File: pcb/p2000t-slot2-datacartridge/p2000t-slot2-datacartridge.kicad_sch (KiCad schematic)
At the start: 27 parts, among them J1 P2000T Port 2, U1 74HC04, U11 CY62256-70PC, U13 74HC173, U14 ZIF, U15 74HC02, U3 74HC138, U4 74HC21, U5 SST39SF040, U6 74HC02, U8 74HC273, U9 74HC273

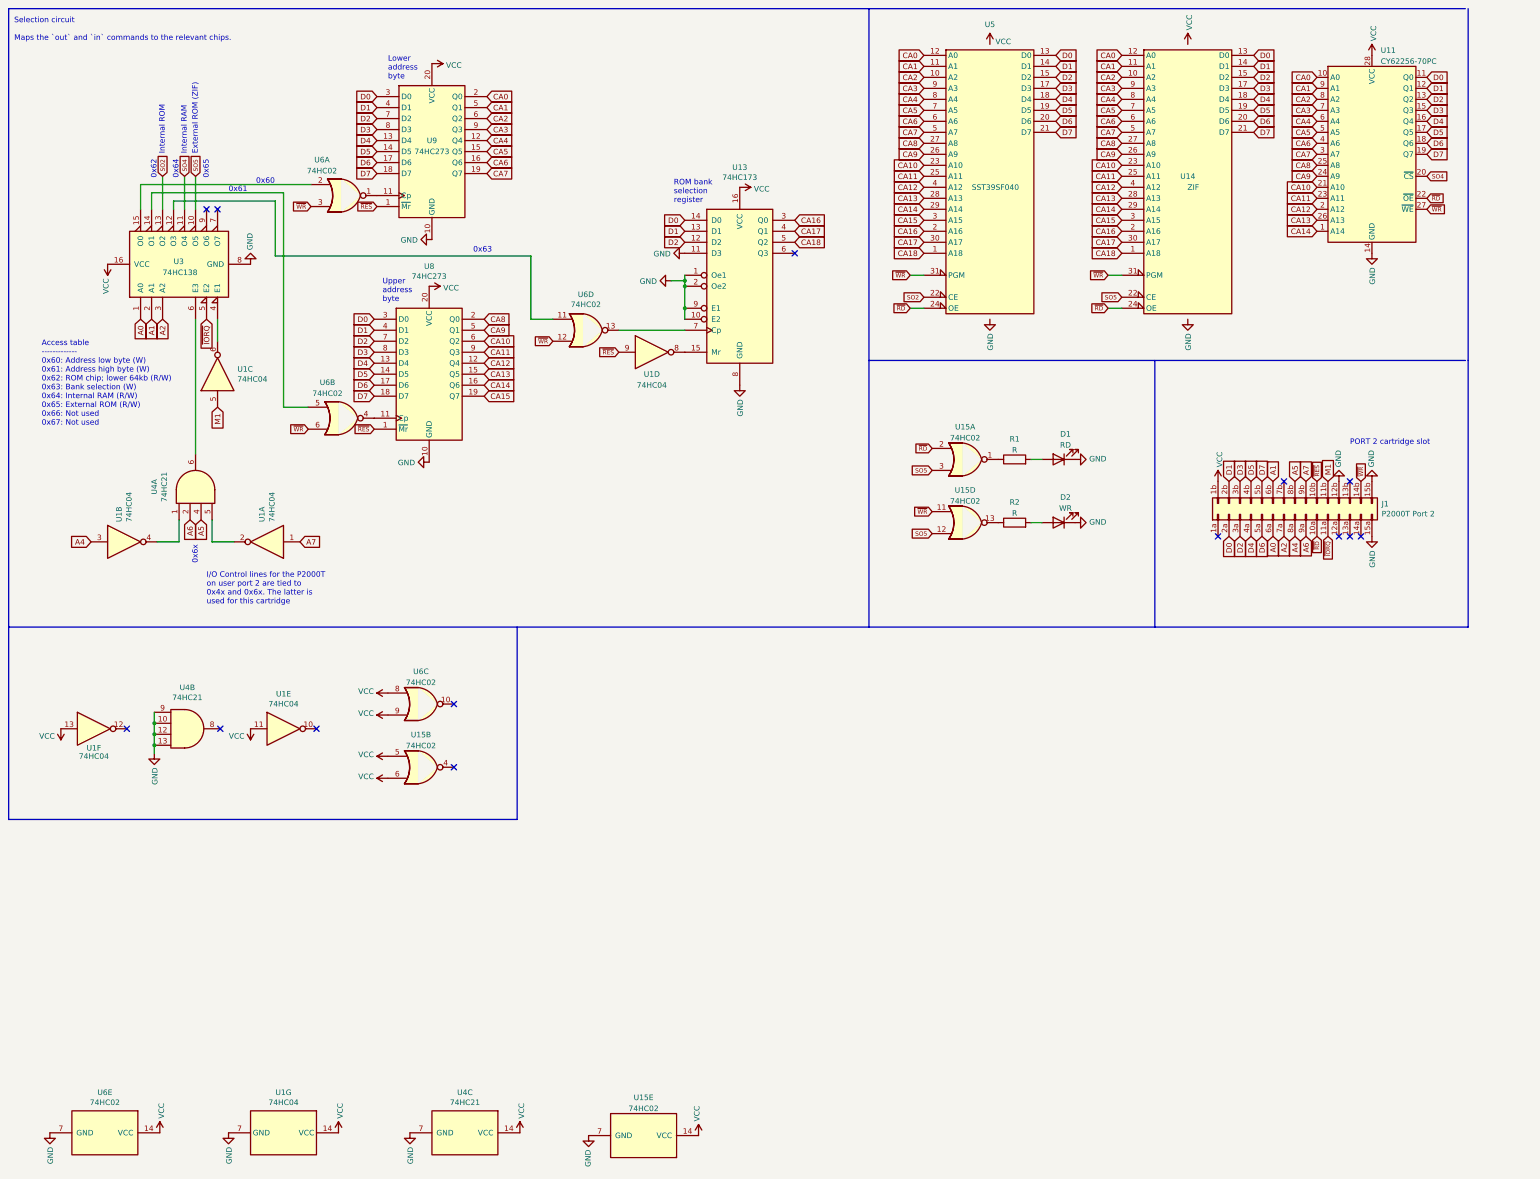
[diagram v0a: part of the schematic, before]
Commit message: Improving lay-out board
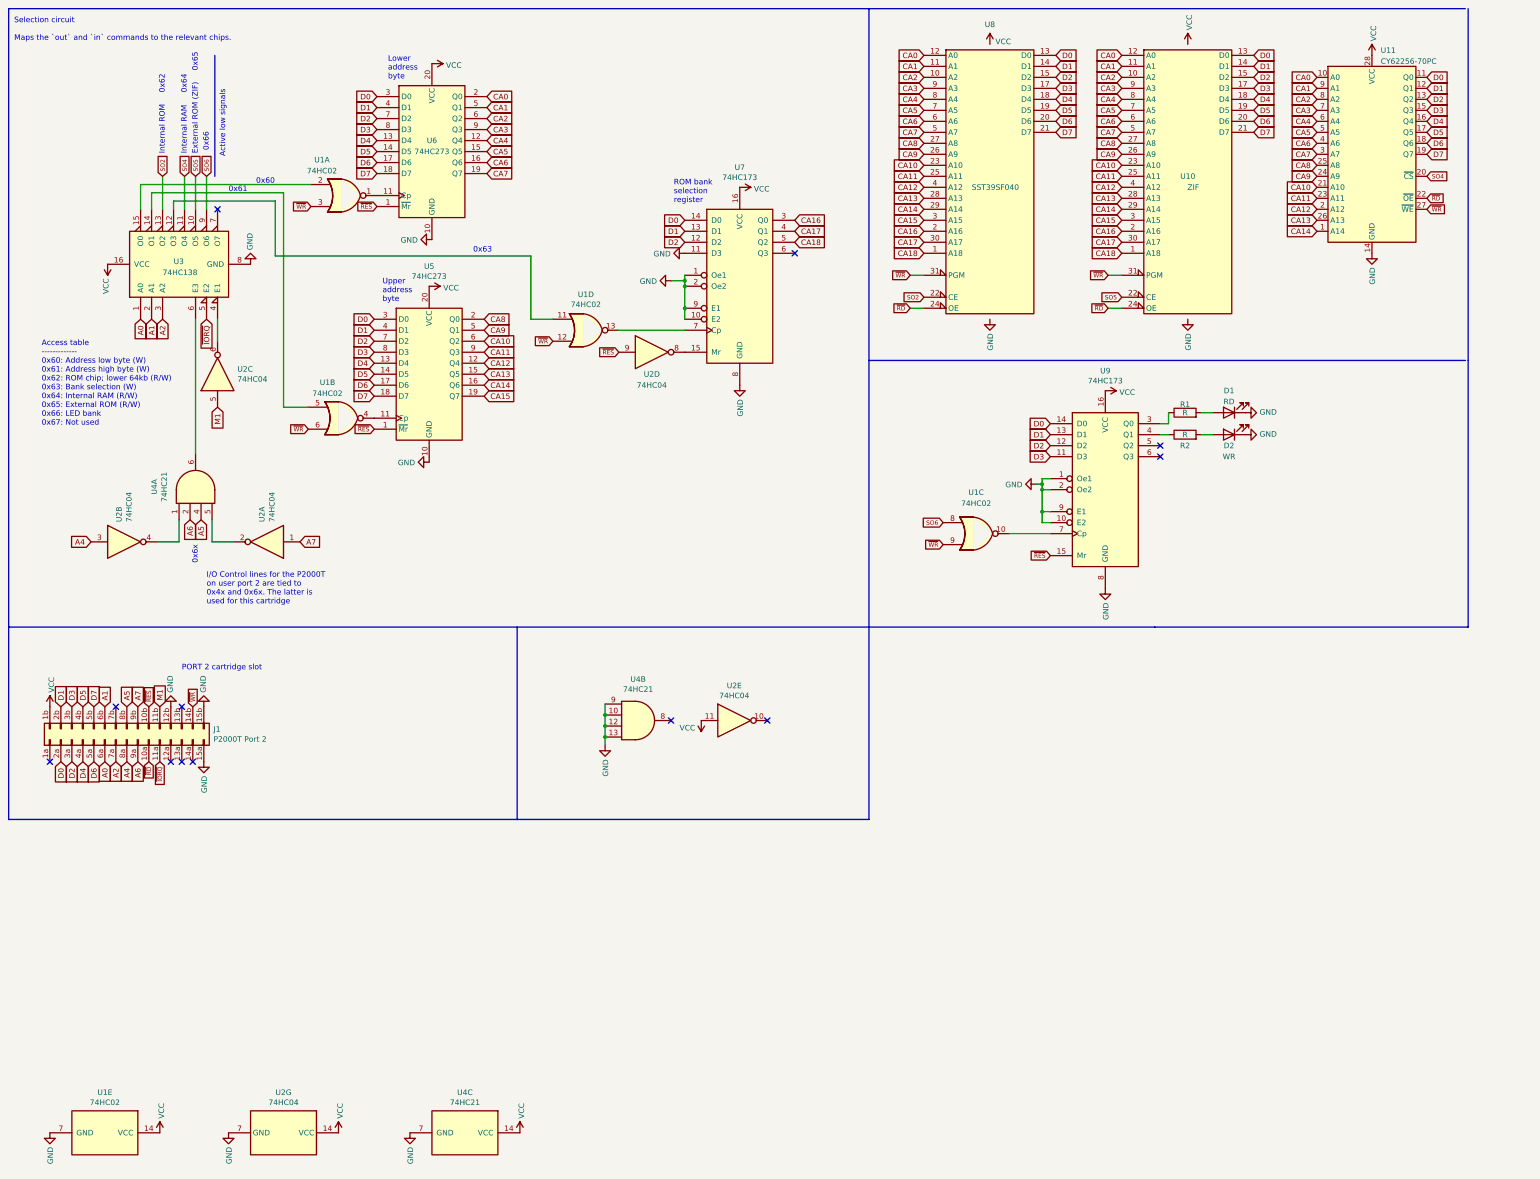
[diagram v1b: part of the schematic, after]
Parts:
- removed unit 6 of U1
- removed U15: 74HC02, Package_DIP:DIP-14_W7.62mm_Socket, symbol 74xx:74HC02
- removed unit 3 of U6
- added unit 3 of U1
- added U9: 74HC173, Package_DIP:DIP-16_W7.62mm_Socket, symbol 74xx:74LS173
- renumbered U6 to U1, U14 to U10, U1 to U2, U8 to U5, U9 to U6, U13 to U7, U5 to U8
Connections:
- net D0: now also U9.14 (D0)
- net D1: now also U9.13 (D1)
- net D2: now also U9.12 (D2)
- net D3: now also U9.11 (D3)
- net GND: now also U9.1 (Oe1), U9.10 (E2), U9.2 (Oe2), U9.8 (GND), U9.9 (E1)
- net VCC: now also U9.16 (VCC)
- net ~{RES}: now also U9.15 (Mr)
- net ~{WR}: now also U1.9
- net SO6: now reaches U3.9 (O6)
- net SO6: now also U1.8
- net at R1.1: now also U9.3 (Q0)
- net at R2.1: now also U9.4 (Q1)
- new net: U1.10, U9.7 (Cp)
- no-connect marks 14 -> 12
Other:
- note added: "0x66"
- note added: "Access table ------------- 0x60: Address low byte (W) 0x61: Address high byte (W) 0x62: ROM chip; lower 64kb (R/W) 0x63: Bank selection (W) 0x64: Internal RAM (R/W) 0x65: External ROM (R/W) 0x66: LED bank 0x67: Not used"
- note added: "Active low signals"
- note removed: "Access table ------------- 0x60: Address low byte (W) 0x61: Address high byte (W) 0x62: ROM chip; lower 64kb (R/W) 0x63: Bank selection (W) 0x64: Internal RAM (R/W) 0x65: External ROM (R/W) 0x66: Not used 0x67: Not used"
- moved on the sheet: D1, D2, J1, R1, R2, U2E, U4B

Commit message: Initial commit rev2 and implementing LEDs in firmware flasher
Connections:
- net VCC: no longer U2.11
- net ~{RES}: now also U2.11; no longer U9.15 (Mr)
- net at U2.10: now also U9.15 (Mr)
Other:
- moved on the sheet: C1, C10, C11, C2, C3, C4, C5, C6, C7, C8, C9, U1E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

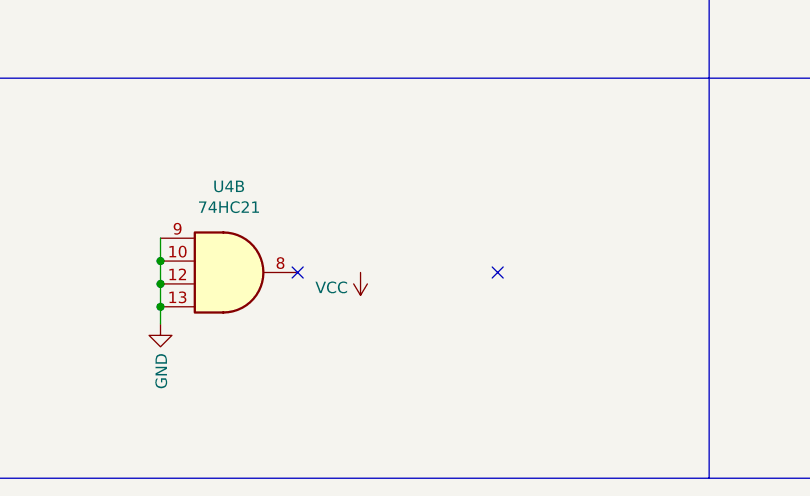
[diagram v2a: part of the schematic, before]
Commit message: Fixing incorrect RES line
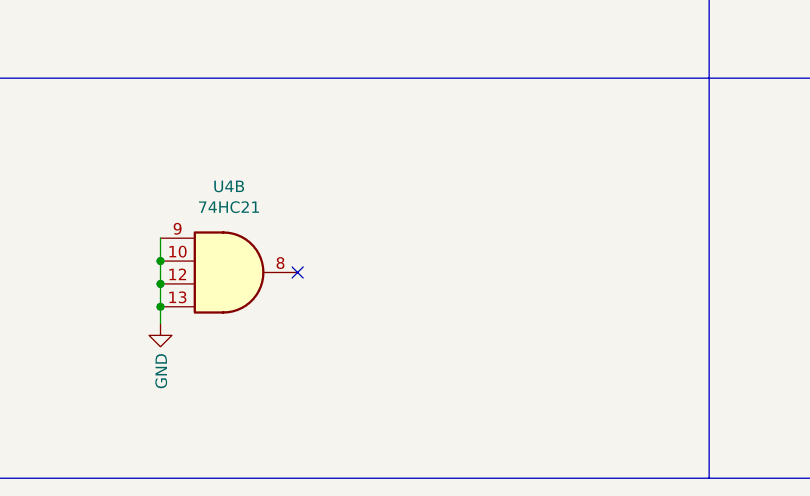
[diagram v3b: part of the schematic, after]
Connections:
- no-connect marks 12 -> 11
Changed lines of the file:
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@@
   (no_connect (at 54.61 189.23))
   (no_connect (at 167.64 179.705))
-  (no_connect (at 189.865 179.705))
   (no_connect (at 57.15 189.23))
   (no_connect (at 52.07 189.23))
@@
     (pin "2")
   )
-  (symbol (lib_id "power:VCC") (at 174.625 179.705 180) (unit 1)
-    (in_bom yes) (on_board yes) (fields_autoplaced)
-    (property "Reference" "#PWR020" (id 0) (at 174.625 175.895 0)
-      (effects (font (size 1.27 1.27)) hide)
-    )
-    (property "Value" "VCC" (id 1) (at 173.228 181.4088 0)
-      (effects (font (size 1.27 1.27)) (justify left))
-    )
-    (property "Footprint" "" (id 2) (at 174.625 179.705 0)
-      (effects (font (size 1.27 1.27)) hide)
-    )
-    (property "Datasheet" "" (id 3) (at 174.625 179.705 0)
-      (effects (font (size 1.27 1.27)) hide)
-    )
-    (pin "1")
-  )
   (symbol (lib_id "power:GND") (at 329.565 71.755 0) (unit 1)
     (in_bom yes) (on_board yes)
@@
       (reference "#PWR019") (unit 1) (value "GND") (footprint "")
     )
-    (path "/138cabe3-0f37-4bdf-9884-6db95dacc365"
-      (reference "#PWR020") (unit 1) (value "VCC") (footprint "")
-    )
     (path "/00000000-0000-0000-0000-0000633bfb64"

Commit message: Building rev2 of the data cartridge
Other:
- note added: "32kb RAM"
- note added: "Access table ------------- 0x60: Address low byte (W) 0x61: Address high byte (W) 0x62: ROM chip; lower 64kb (R/W) 0x63: Bank selection (W) 0x64: RAM (R/W) 0x65: External ROM (R/W) 0x66: LED bank 0x67: Not used"
- note added: "External ROM via ZIF socket"
- note added: "LED bank"
- note added: "ROM & RAM"
- note added: "Software-controlled RD and WR LEDs"
- note added: "Tie unused gates to GND/VCC"
- note removed: "Access table ------------- 0x60: Address low byte (W) 0x61: Address high byte (W) 0x62: ROM chip; lower 64kb (R/W) 0x63: Bank selection (W) 0x64: Internal RAM (R/W) 0x65: External ROM (R/W) 0x66: LED bank 0x67: Not used"
- moved on the sheet: C1, C10, C11, C2, C3, C4, C5, C6, C7, C8, C9, U1A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
